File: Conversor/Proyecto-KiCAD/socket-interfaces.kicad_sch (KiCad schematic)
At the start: 24 parts, among them J10 DIMM100, P10 Header GPIO, P11 Header SD, P5 Header 7X2, P6 Header UART, P7 Header I2C, P8 Header PWM, P9 Header ADC, SW1 Switch, SW2 Switch, SW3 Switch, SW4 Switch

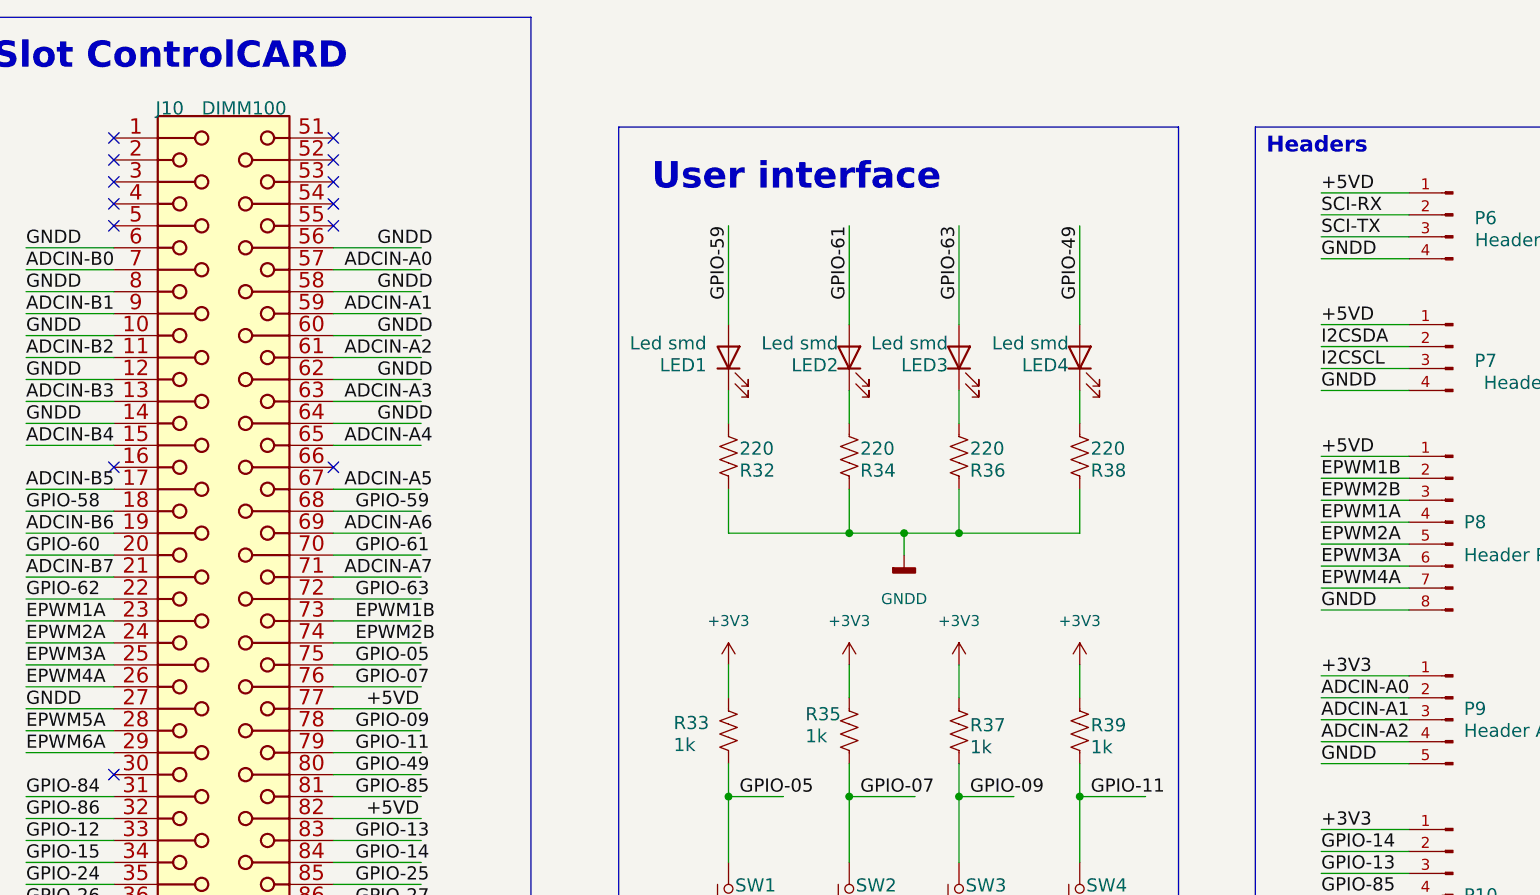
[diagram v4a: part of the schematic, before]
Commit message: Terminar el resto de los cambios de Jorge
- Capacitores electroliticos para el circuito de bootstrap, en paralelo
a los cerámicos
- Cambiar el I2C a 3V3 del lado digital
- Hacer la separacion de linea de datos de I2C del lado digital como en
la nota de aplicación SLYT403A
- Dejar el Vaux del LM5056A con un jumper por si acaso
- Lo mismo con la resistencia de dead-time RDT de los drivers, dejar una
footprint de resistencia SMD para poder cambiarlas de ser necesario
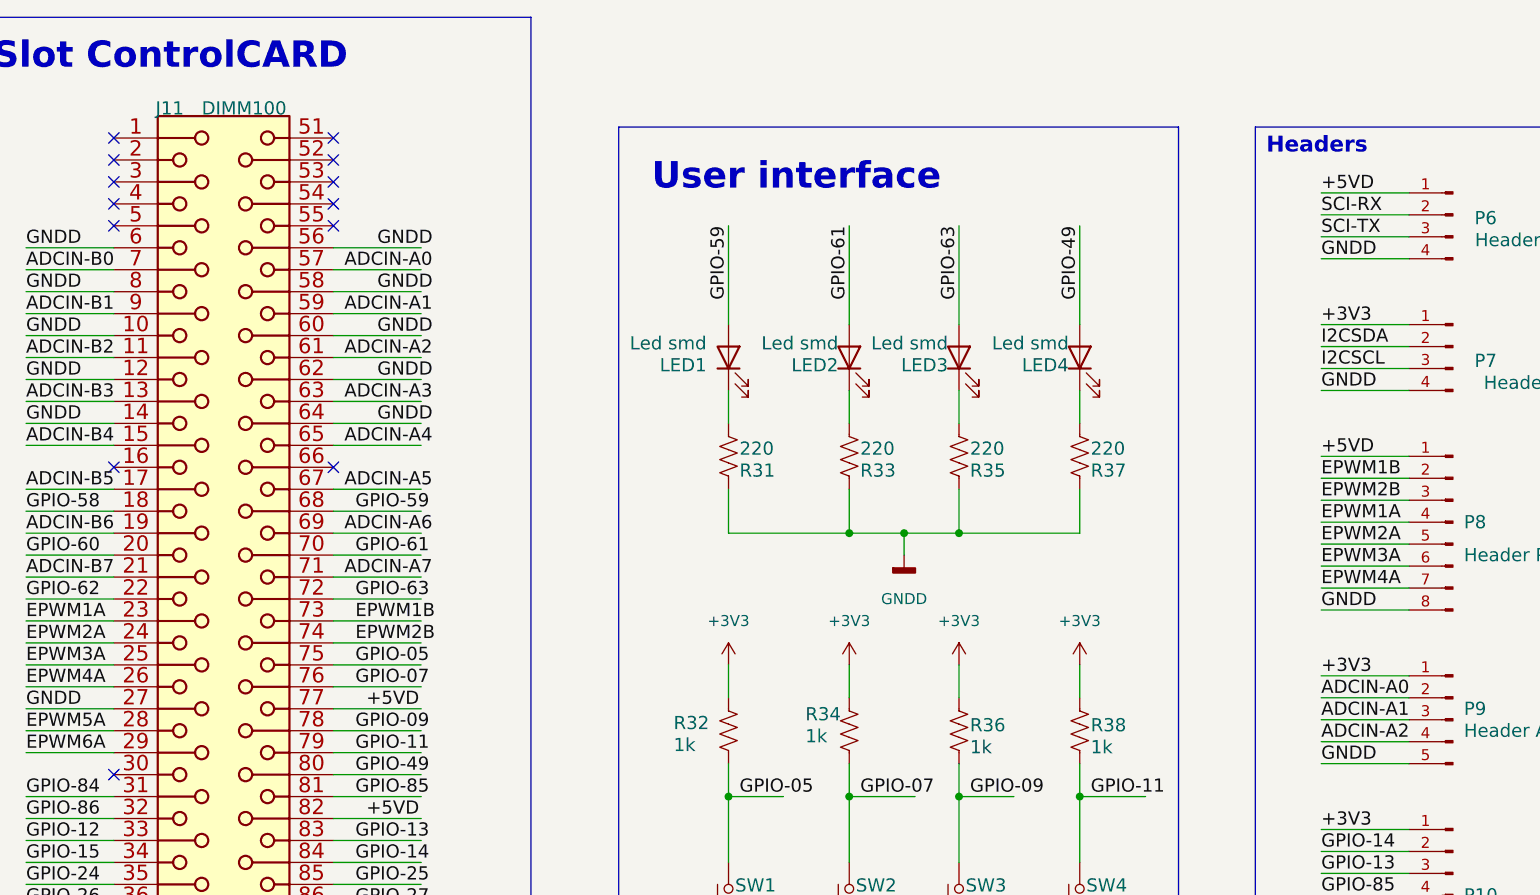
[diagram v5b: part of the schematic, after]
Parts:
- renumbered J10 to J11, R32 to R31, R33 to R32, R34 to R33, R35 to R34, R36 to R35, R37 to R36, R38 to R37, R39 to R38
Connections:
- net +3V3: now also P7.1 (Pin_1)
- net +5VD: no longer P7.1 (Pin_1)
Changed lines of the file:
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@@
     (effects (font (size 1.524 1.524)) (justify left bottom))
   )
-  (label "+5VD" (at 175.26 50.8 0)
+  (label "+3V3" (at 175.26 50.8 0)
     (effects (font (size 1.524 1.524)) (justify left bottom))
   )
@@
   (symbol (lib_id "power:+3V3") (at 133.35 90.17 0) (unit 1)
     (in_bom yes) (on_board yes) (fields_autoplaced)
-    (property "Reference" "#PWR088" (id 0) (at 133.35 93.98 0)
+    (property "Reference" "#PWR080" (id 0) (at 133.35 93.98 0)
       (effects (font (size 1.27 1.27)) hide)
     )
@@
   (symbol (lib_id "Device:R_US") (at 133.35 97.79 180) (unit 1)
     (in_bom yes) (on_board yes)
-    (property "Reference" "R37" (id 0) (at 134.62 98.044 0)
+    (property "Reference" "R36" (id 0) (at 134.62 98.044 0)
       (effects (font (size 1.524 1.524)) (justify right top))
     )
@@
   (symbol (lib_id "power:+3V3") (at 120.65 90.17 0) (unit 1)
     (in_bom yes) (on_board yes) (fields_autoplaced)
-    (property "Reference" "#PWR085" (id 0) (at 120.65 93.98 0)
+    (property "Reference" "#PWR077" (id 0) (at 120.65 93.98 0)
       (effects (font (size 1.27 1.27)) hide)
     )
@@
   (symbol (lib_id "Device:R_US") (at 120.65 66.04 0) (unit 1)
     (in_bom yes) (on_board yes)
-    (property "Reference" "R34" (id 0) (at 121.92 68.58 0)
+    (property "Reference" "R33" (id 0) (at 121.92 68.58 0)
       (effects (font (size 1.524 1.524)) (justify left bottom))
     )
@@
   (symbol (lib_id "DIMM100:390213-1-") (at 55.88 26.67 270) (unit 1)
     (in_bom yes) (on_board yes)
-    (property "Reference" "J10" (id 0) (at 40.386 26.67 90)
+    (property "Reference" "J11" (id 0) (at 40.386 26.67 90)
       (effects (font (size 1.524 1.524)) (justify left bottom))
     )
@@
   (symbol (lib_id "power:+3V3") (at 147.32 90.17 0) (unit 1)
     (in_bom yes) (on_board yes) (fields_autoplaced)
-    (property "Reference" "#PWR089" (id 0) (at 147.32 93.98 0)
+    (property "Reference" "#PWR081" (id 0) (at 147.32 93.98 0)
       (effects (font (size 1.27 1.27)) hide)
     )
@@
   (symbol (lib_id "Device:R_US") (at 106.68 66.04 0) (unit 1)
     (in_bom yes) (on_board yes)
-    (property "Reference" "R32" (id 0) (at 107.95 68.58 0)
+    (property "Reference" "R31" (id 0) (at 107.95 68.58 0)
       (effects (font (size 1.524 1.524)) (justify left bottom))
     )
@@
   (symbol (lib_id "Device:R_US") (at 147.32 66.04 0) (unit 1)
     (in_bom yes) (on_board yes)
-    (property "Reference" "R38" (id 0) (at 148.59 68.58 0)
+    (property "Reference" "R37" (id 0) (at 148.59 68.58 0)
       (effects (font (size 1.524 1.524)) (justify left bottom))
     )
@@
   (symbol (lib_id "power:GNDD") (at 127 77.47 0) (unit 1)
     (in_bom yes) (on_board yes) (fields_autoplaced)
-    (property "Reference" "#PWR086" (id 0) (at 127 83.82 0)
+    (property "Reference" "#PWR078" (id 0) (at 127 83.82 0)
       (effects (font (size 1.27 1.27)) hide)
     )
@@
   (symbol (lib_id "Device:R_US") (at 120.65 97.79 180) (unit 1)
     (in_bom yes) (on_board yes)
-    (property "Reference" "R35" (id 0) (at 115.57 96.774 0)
+    (property "Reference" "R34" (id 0) (at 115.57 96.774 0)
       (effects (font (size 1.524 1.524)) (justify right top))
     )
@@
   (symbol (lib_id "Device:R_US") (at 133.35 66.04 0) (unit 1)
     (in_bom yes) (on_board yes)
-    (property "Reference" "R36" (id 0) (at 134.62 68.58 0)
+    (property "Reference" "R35" (id 0) (at 134.62 68.58 0)
       (effects (font (size 1.524 1.524)) (justify left bottom))
     )
@@
   (symbol (lib_id "power:+5VD") (at 251.46 36.83 0) (unit 1)
     (in_bom yes) (on_board yes) (fields_autoplaced)
-    (property "Reference" "#PWR090" (id 0) (at 251.46 40.64 0)
+    (property "Reference" "#PWR082" (id 0) (at 251.46 40.64 0)
       (effects (font (size 1.27 1.27)) hide)
     )
@@
   (symbol (lib_id "power:GNDD") (at 264.16 40.64 0) (unit 1)
     (in_bom yes) (on_board yes) (fields_autoplaced)
-    (property "Reference" "#PWR092" (id 0) (at 264.16 46.99 0)
+    (property "Reference" "#PWR084" (id 0) (at 264.16 46.99 0)
       (effects (font (size 1.27 1.27)) hide)
     )
@@
   (symbol (lib_id "power:+3V3") (at 106.68 90.17 0) (unit 1)
     (in_bom yes) (on_board yes) (fields_autoplaced)
-    (property "Reference" "#PWR084" (id 0) (at 106.68 93.98 0)
+    (property "Reference" "#PWR076" (id 0) (at 106.68 93.98 0)
       (effects (font (size 1.27 1.27)) hide)
     )
@@
   (symbol (lib_id "power:+3V3") (at 257.81 36.83 0) (unit 1)
     (in_bom yes) (on_board yes) (fields_autoplaced)
-    (property "Reference" "#PWR091" (id 0) (at 257.81 40.64 0)
+    (property "Reference" "#PWR083" (id 0) (at 257.81 40.64 0)
       (effects (font (size 1.27 1.27)) hide)
     )
@@
   (symbol (lib_id "Device:R_US") (at 147.32 97.79 180) (unit 1)
     (in_bom yes) (on_board yes)
-    (property "Reference" "R39" (id 0) (at 148.59 98.044 0)
+    (property "Reference" "R38" (id 0) (at 148.59 98.044 0)
       (effects (font (size 1.524 1.524)) (justify right top))
     )
@@
   (symbol (lib_id "Device:R_US") (at 106.68 97.79 180) (unit 1)
     (in_bom yes) (on_board yes)
-    (property "Reference" "R33" (id 0) (at 100.33 97.79 0)
+    (property "Reference" "R32" (id 0) (at 100.33 97.79 0)
       (effects (font (size 1.524 1.524)) (justify right top))
     )
@@
   (symbol (lib_id "power:GNDD") (at 127 125.73 0) (unit 1)
     (in_bom yes) (on_board yes) (fields_autoplaced)
-    (property "Reference" "#PWR087" (id 0) (at 127 132.08 0)
-      (effects (font (size 1.27 1.27)) hide)
-    )
+    (property "Reference" "#PWR079" (id 0) (at 127 132.08 0)
+      (effects (font (size 1.27 1.27)) hide)
+    )
